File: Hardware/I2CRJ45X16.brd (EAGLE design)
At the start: 146 x 50 mm, 90 parts, among them IC1 MCP23017SO, IC2 MCP23017SO, IC3 MCP23017SO, IC4 MCP23017SO, J1 RJ45-X8, J2 RJ45-X8, J4 I2C-BREAKOUT, J6 I2C-BREAKOUT

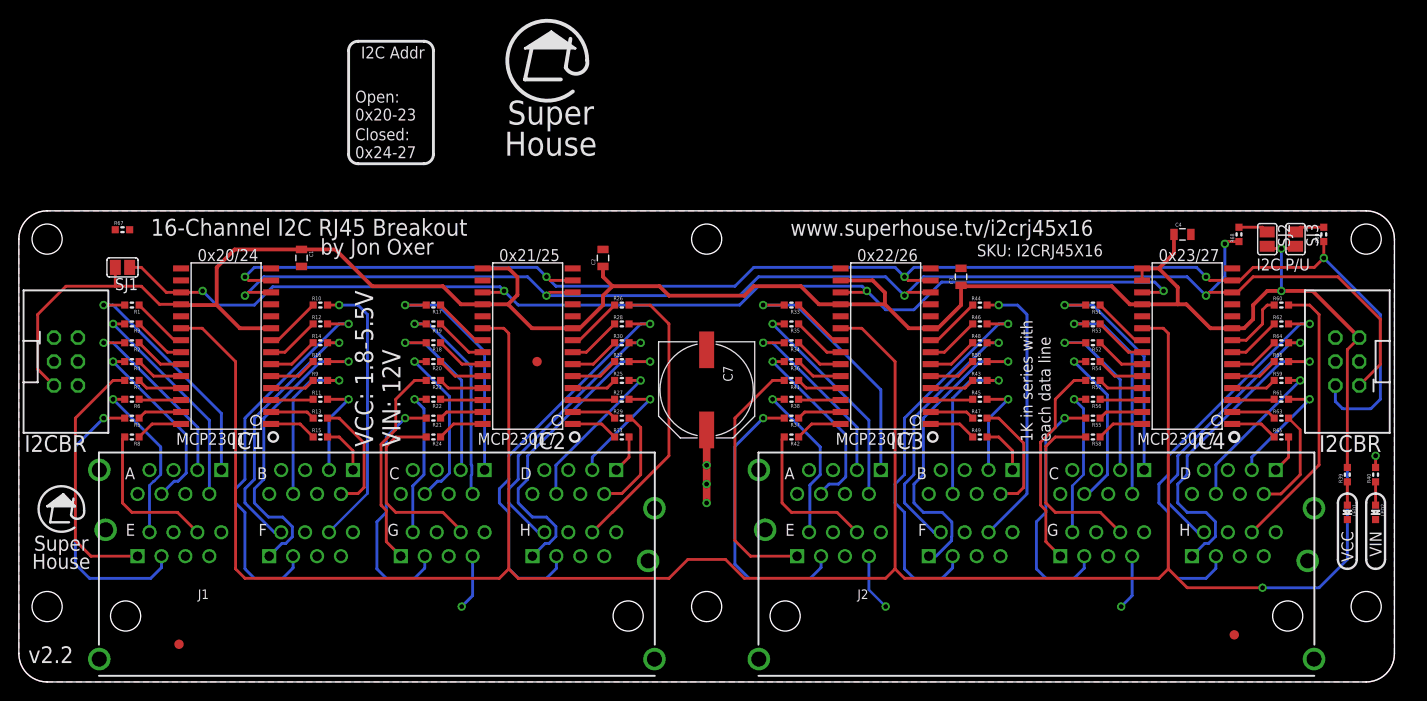
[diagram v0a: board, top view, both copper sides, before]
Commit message: Replaced project files with major redesign for v3.0 release.
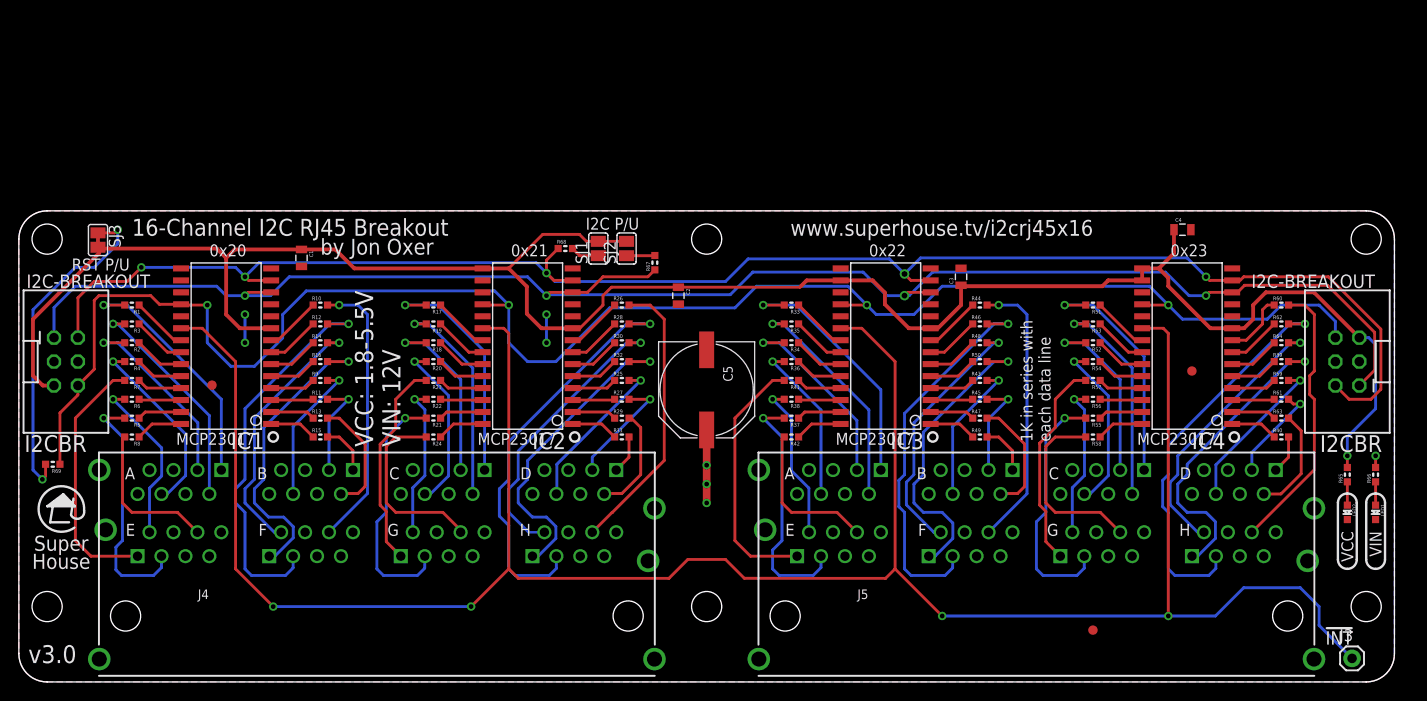
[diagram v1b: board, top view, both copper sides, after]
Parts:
- removed J6: I2C-BREAKOUT, SuperHouse-Connectors:2X03-SHROUDED
- added J3: M01-PLAIN, SuperHouse-Connectors:1X01
- added J5: RJ45-X8, SuperHouse-Connectors:RJ45-2X4
- C5: value 330uF -> 330uF 50V
- FID1, FID2, FID3: device freetronics:FIDUCIAL-1X2.5 -> SuperHouse-Symbols:FIDUCIAL-1X2.5
- J1, J2: value RJ45-X8 -> I2C-BREAKOUT; device SuperHouse-Connectors:RJ45-2X4 -> SuperHouse-Connectors:2X03-SHROUDED
- J4: value I2C-BREAKOUT -> RJ45-X8; device SuperHouse-Connectors:2X03-SHROUDED -> SuperHouse-Connectors:RJ45-2X4
- LED1: value BLUE -> GREEN
- LED2: value GREEN -> BLUE
- R39, R40: value 4K7 -> 1K
- R65, R66: value 1K -> 4K7
- R67, R68: value 10K -> 4K7
- R69: value 10K -> 22K
- SJ1: value I2C Address -> SDA PU
- SJ3: value SDA PU -> RST-PU; device SuperHouse-Jumpers:SJ -> SuperHouse-Jumpers:SJC
- moved R69 137.1 mm to (3.60, 23.1), turned to 180 degrees
- moved SJ3 127.1 mm to (8.40, 46.9)
- moved FID1 111.7 mm to (20.5, 31.5)
- moved FID2 111.3 mm to (124.5, 33.0)
- moved R68 71.5 mm to (58.0, 46.0), turned to 0 degrees
- moved SJ2 68.0 mm to (64.5, 46.0), turned to 90 degrees
- moved FID3 65.5 mm to (114.0, 5.50)
- moved R67 56.6 mm to (67.5, 44.5), turned to 90 degrees
- moved SJ1 50.5 mm to (61.5, 46.0), turned to 90 degrees
- moved J1 42.6 mm to (5.00, 34.0)
- moved J2 42.6 mm to (141.0, 34.0), turned to 180 degrees
- moved J4 42.6 mm to (38.0, 7.00)
- moved R66 15.6 mm to (144.0, 22.0), turned to 90 degrees
- moved R39 13.9 mm to (134.0, 34.0), turned to 0 degrees
- moved R40 10.8 mm to (134.0, 26.0), turned to 0 degrees
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- renumbered C7 to C5
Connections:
- removed net ADDR2: IC1.17, IC2.17, IC3.17, IC4.17, R67.2, SJ1.1
- new net N$2: R68.2, SJ1.1
- net !INT: now also J3.1
- net !RESET: now also IC1.18, IC2.18, IC3.18, IC4.18, J1.6, J2.6, R69.1; no longer J4.6, J6.6
- net 1A1: now also J4.A1; no longer J1.A1
- net 1A2: now also J4.A2; no longer J1.A2
- net 1A3: now also J4.A3; no longer J1.A3
- net 1A6: now also J4.A6; no longer J1.A6
- net 1B1: now also J4.B1; no longer J1.B1
- net 1B2: now also J4.B2; no longer J1.B2
- net 1B3: now also J4.B3; no longer J1.B3
- net 1B6: now also J4.B6; no longer J1.B6
- net 1C1: now also J4.C1; no longer J1.C1
- net 1C2: now also J4.C2; no longer J1.C2
- net 1C3: now also J4.C3; no longer J1.C3
- net 1C6: now also J4.C6; no longer J1.C6
- net 1D1: now also J4.D1; no longer J1.D1
- net 1D2: now also J4.D2; no longer J1.D2
- net 1D3: now also J4.D3; no longer J1.D3
- net 1D6: now also J4.D6; no longer J1.D6
- net 1E1: now also J4.E1; no longer J1.E1
- net 1E2: now also J4.E2; no longer J1.E2
- net 1E3: now also J4.E3; no longer J1.E3
- net 1E6: now also J4.E6; no longer J1.E6
- net 1F1: now also J4.F1; no longer J1.F1
- net 1F2: now also J4.F2; no longer J1.F2
- net 1F3: now also J4.F3; no longer J1.F3
- net 1F6: now also J4.F6; no longer J1.F6
- net 1G1: now also J4.G1; no longer J1.G1
- net 1G2: now also J4.G2; no longer J1.G2
- net 1G3: now also J4.G3; no longer J1.G3
- net 1G6: now also J4.G6; no longer J1.G6
- net 1H1: now also J4.H1; no longer J1.H1
- net 1H2: now also J4.H2; no longer J1.H2
- net 1H3: now also J4.H3; no longer J1.H3
- net 1H6: now also J4.H6; no longer J1.H6
- net 2A1: now also J5.A1; no longer J2.A1
- net 2A2: now also J5.A2; no longer J2.A2
- net 2A3: now also J5.A3; no longer J2.A3
- net 2A6: now also J5.A6; no longer J2.A6
- net 2B1: now also J5.B1; no longer J2.B1
- net 2B2: now also J5.B2; no longer J2.B2
- net 2B3: now also J5.B3; no longer J2.B3
- net 2B6: now also J5.B6; no longer J2.B6
- net 2C1: now also J5.C1; no longer J2.C1
- net 2C2: now also J5.C2; no longer J2.C2
- net 2C3: now also J5.C3; no longer J2.C3
- net 2C6: now also J5.C6; no longer J2.C6
- net 2D1: now also J5.D1, R40.2; no longer J2.D1, R65.2
- net 2D2: now also J5.D2; no longer J2.D2
- net 2D3: now also J5.D3; no longer J2.D3
- net 2D6: now also J5.D6; no longer J2.D6
- net 2E1: now also J5.E1; no longer J2.E1
- net 2E2: now also J5.E2; no longer J2.E2
- net 2E3: now also J5.E3; no longer J2.E3
- net 2E6: now also J5.E6; no longer J2.E6
- net 2F1: now also J5.F1; no longer J2.F1
- net 2F2: now also J5.F2; no longer J2.F2
- net 2F3: now also J5.F3; no longer J2.F3
- net 2F6: now also J5.F6; no longer J2.F6
- net 2G1: now also J5.G1; no longer J2.G1
- net 2G2: now also J5.G2; no longer J2.G2
- net 2G3: now also J5.G3; no longer J2.G3
- net 2G6: now also J5.G6; no longer J2.G6
- net 2H1: now also J5.H1, R39.2; no longer J2.H1, R66.2
- net 2H2: now also J5.H2; no longer J2.H2
- net 2H3: now also J5.H3; no longer J2.H3
- net 2H6: now also J5.H6; no longer J2.H6
- net GND: now also IC1.17, IC2.17, IC3.17, IC4.17, J1.4, J2.4, J4.A7, J4.A8, J4.B7, J4.B8, J4.C7, J4.C8, J4.D7, J4.D8, J4.E7, J4.E8, J4.F7, J4.F8, J4.G7, J4.G8, J4.GND0, J4.GND1, J4.GND2, J4.GND3, J4.GND4, J4.GND5, J4.H7, J4.H8, J5.A7, J5.A8, J5.B7, J5.B8, J5.C7, J5.C8, J5.D7, J5.D8, J5.E7, J5.E8, J5.F7, J5.F8, J5.G7, J5.G8, J5.GND0, J5.GND1, J5.GND2, J5.GND3, J5.GND4, J5.GND5, J5.H7, J5.H8; no longer J1.A7, J1.A8, J1.B7, J1.B8, J1.C7, J1.C8, J1.D7, J1.D8, J1.E7, J1.E8, J1.F7, J1.F8, J1.G7, J1.G8, J1.GND0, J1.GND1, J1.GND2, J1.GND3, J1.GND4, J1.GND5, J1.H7, J1.H8, J2.A7, J2.A8, J2.B7, J2.B8, J2.C7, J2.C8, J2.D7, J2.D8, J2.E7, J2.E8, J2.F7, J2.F8, J2.G7, J2.G8, J2.GND0, J2.GND1, J2.GND2, J2.GND3, J2.GND4, J2.GND5, J2.H7, J2.H8, J4.4, J6.4, R67.1
- net GPB0-4: now also R40.1; no longer R65.1
- net GPB4-4: now also R39.1; no longer R66.1
- net N$1: now also R67.2; no longer R68.2
- net N$7: now also LED2.A, R65.1; no longer LED1.A, R39.1
- net N$8: now also LED1.A, R66.1; no longer LED2.A, R40.1
- net SCL: now also J1.1, J2.1, R67.1; no longer J4.1, J6.1, R68.1
- net SDA: now also J1.2, J2.2, R68.1; no longer J4.2, J6.2, R69.1
- net VCC: now also J1.5, J2.5, R65.2; no longer IC1.18, IC2.18, IC3.18, IC4.18, J4.5, J6.5, R39.2
- net VIN: now also J1.3, J2.3, J4.A4, J4.A5, J4.B4, J4.B5, J4.C4, J4.C5, J4.D4, J4.D5, J4.E4, J4.E5, J4.F4, J4.F5, J4.G4, J4.G5, J4.H4, J4.H5, J5.A4, J5.A5, J5.B4, J5.B5, J5.C4, J5.C5, J5.D4, J5.D5, J5.E4, J5.E5, J5.F4, J5.F5, J5.G4, J5.G5, J5.H4, J5.H5, R66.2; no longer J1.A4, J1.A5, J1.B4, J1.B5, J1.C4, J1.C5, J1.D4, J1.D5, J1.E4, J1.E5, J1.F4, J1.F5, J1.G4, J1.G5, J1.H4, J1.H5, J2.A4, J2.A5, J2.B4, J2.B5, J2.C4, J2.C5, J2.D4, J2.D5, J2.E4, J2.E5, J2.F4, J2.F5, J2.G4, J2.G5, J2.H4, J2.H5, J4.3, J6.3, R40.2
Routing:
- net !RESET: track 0.00 -> 185.3 mm, vias 0 -> 4
- net ADDR2: track 124.1 -> 0.00 mm, vias 4 -> 0
- net N$3: track 3.21 -> 35.8 mm, vias 0 -> 2
- net SCL: track 152.8 -> 177.8 mm, vias 5 -> 4
- net SDA: track 154.2 -> 176.0 mm
- net GND: track 17.7 -> 6.00 mm, vias 3 -> 4
- net VCC: track 232.7 -> 223.5 mm, vias 2 -> 1
- net 1E3: track 30.4 -> 26.1 mm
- net 2E3: track 30.4 -> 26.5 mm
- net N$2: track 0.00 -> 3.05 mm
- net 2A6: track 20.2 -> 17.4 mm
- net 2B6: track 17.1 -> 15.3 mm
- net 1B6: track 17.1 -> 15.3 mm
- net 2D3: track 12.3 -> 10.6 mm
- net 2H1: track 34.5 -> 33.1 mm
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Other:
- board text added: "!INT"
- board text added: "!RST"
- board text added: "0x20"
- board text added: "0x21"
- board text added: "0x22"
- board text added: "0x23"
- board text added: "24-Channel I2C RJ45 Breakout"
- board text added: "Copyright 2019-2021 SuperHouse Automation Pty Ltd Released under the terms of the TAPR Open Hardware License: www.tapr.org/OHL"
- board text added: "GND"
- board text added: "I2C-BREAKOUT"
- board text added: "RJ45 Pinout"
- board text added: "RST P/U"
- board text added: "SCL"
- board text added: "SDA"
- board text added: "v3.0"
- board text added: "www.superhouse.tv"
- board text removed: "0x20/24"
- board text removed: "0x21/25"
- board text removed: "0x22/26"
- board text removed: "0x23/27"
- board text removed: "Closed: 0x24-27"
- board text removed: "Copyright 2019 SuperHouse Automation Pty Ltd Released under the terms of the TAPR Open Hardware License: www.tapr.org/OHL"
- board text removed: "I2C Addr"
- board text removed: "Open: 0x20-23"
- board text removed: "RJ45 Pinout:"
- board text removed: "v2.2"

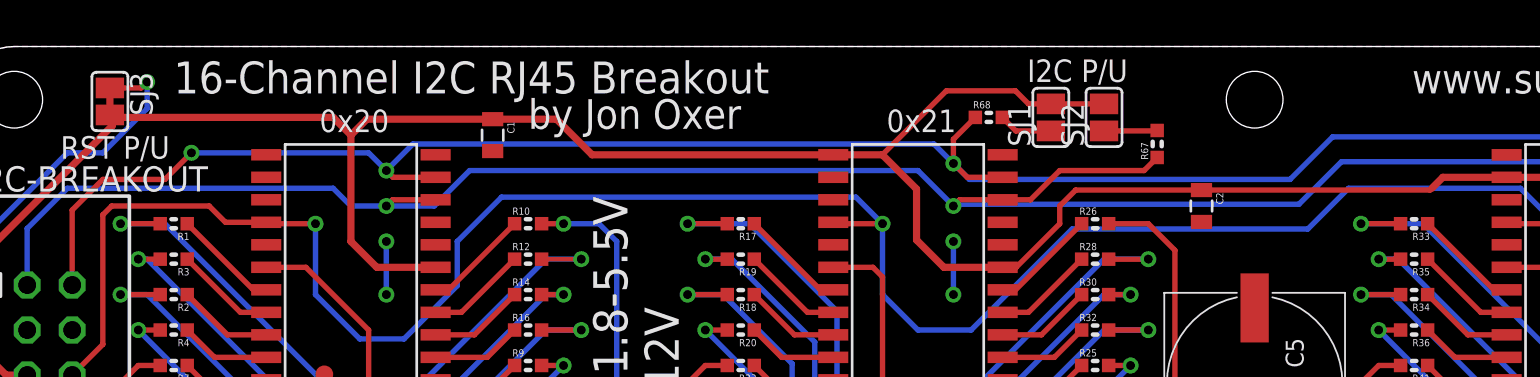
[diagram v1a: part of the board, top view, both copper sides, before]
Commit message: Major rework based on 24-port version.
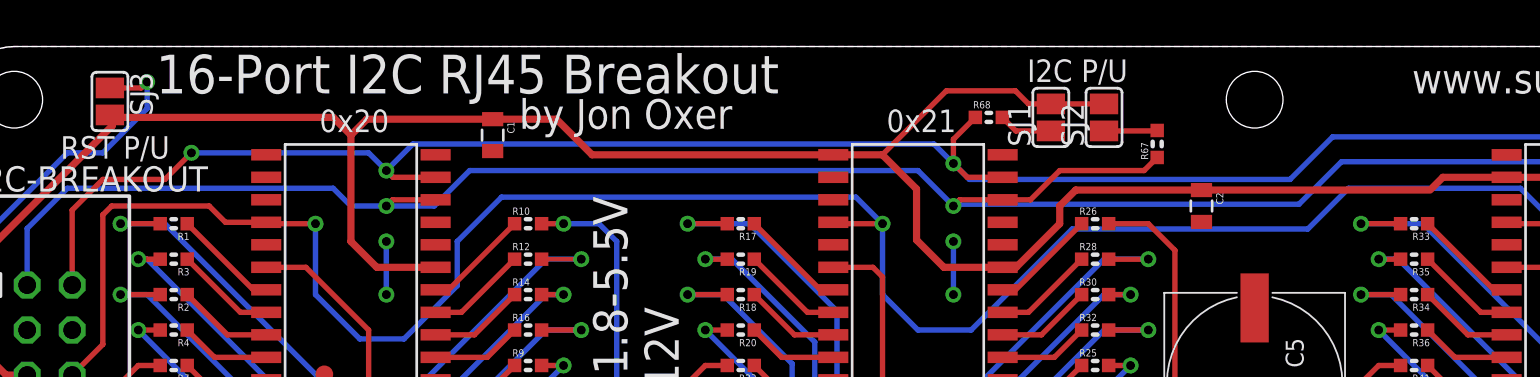
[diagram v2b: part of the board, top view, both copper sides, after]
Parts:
- R69: value 22K -> 10K
- SJ3: device SuperHouse-Jumpers:SJC -> SuperHouse-Jumpers:SJ
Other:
- board text added: "16-Port I2C RJ45 Breakout"
- board text removed: "16-Channel I2C RJ45 Breakout"
- board text removed: "24-Channel I2C RJ45 Breakout"
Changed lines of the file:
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@@
 </layers>
 <board>
-<fusionsync huburn="a.cGVyc29uYWw6dWUyZDliZmNi" projecturn="a.cGVyc29uYWw6dWUyZDliZmNiIzIwMTkwMzE1MTgyMjY5OTA2" f3durn="urn:adsk.wipprod:dm.lineage:_H2PRmvNSomCkomNSTRBxw" pcbguid="e014f554-0983-42e7-88b6-f6e08b18e2c7" lastpulledtime="" lastsyncedchangeguid="1491f9b9-a179-9c0a-9821-19275fe4b9b0" latestrevisionid="" lastsyncedrevisionid="" lastboardhashguid="57911f44-b240-5674-ec1f-8acbffdfcb08" lastpushedtime="2021-04-15T04:03:47Z" linktopcb3d="false"/>
+<fusionsync huburn="a.cGVyc29uYWw6dWUyZDliZmNi" projecturn="a.cGVyc29uYWw6dWUyZDliZmNiIzIwMTkwMzE1MTgyMjY5OTA2" f3durn="urn:adsk.wipprod:dm.lineage:_H2PRmvNSomCkomNSTRBxw" pcbguid="e014f554-0983-42e7-88b6-f6e08b18e2c7" lastpulledtime="" lastsyncedchangeguid="1491f9b9-a179-9c0a-9821-19275fe4b9b0" latestrevisionid="" lastsyncedrevisionid="" lastboardhashguid="9f721456-5d46-4459-276f-f39935e09a9c" lastpushedtime="2021-04-15T05:54:07Z" linktopcb3d="false"/>
 <plain>
 <wire x1="3" y1="0" x2="0" y2="3" width="0" layer="20" curve="-90"/>
@@
 <text x="50.045" y="43.854" size="3.1" layer="22" font="vector" ratio="17" distance="30" rot="MR0" align="center-left">Super
 House</text>
-<text x="60.045" y="27" size="2.8" layer="22" font="vector" ratio="17" distance="20" rot="MR0">24-Channel
+<text x="60.045" y="27" size="2.8" layer="22" font="vector" ratio="17" distance="20" rot="MR0">16-Port
 I2C RJ45
 Breakout</text>
@@
 <text x="4.5" y="12" size="1.6" layer="21" font="vector" ratio="17" distance="20" align="bottom-center">Super
 House</text>
-<text x="12" y="47.354" size="1.8" layer="21" font="vector" ratio="17" distance="30">16-Channel I2C RJ45 Breakout</text>
-<text x="32" y="45.354" size="1.6764" layer="21" font="vector" ratio="17" distance="30">by Jon Oxer</text>
+<text x="11" y="47.354" size="2.1844" layer="21" font="vector" ratio="17" distance="30">16-Port I2C RJ45 Breakout</text>
+<text x="31.5" y="45.354" size="1.6764" layer="21" font="vector" ratio="17" distance="30">by Jon Oxer</text>
 <text x="40.5" y="24.955" size="1.9304" layer="21" font="vector" ratio="17" rot="R90">VCC: 1.8-5.5V
 VIN: 12V</text>
@@
 <attribute name="VALUE" x="122.484" y="46.603" size="0.4064" layer="27"/>
 </element>
-<element name="SJ2" library="SuperHouse-Jumpers" library_urn="urn:adsk.eagle:library:12190622" package="SJ" package3d_urn="urn:adsk.eagle:package:7066338/1" value="SCL PU" x="64.5" y="46" smashed="yes" rot="R90">
+<element name="SJ2" library="SuperHouse-Jumpers" library_urn="urn:adsk.eagle:library:12190622" package="SJ" package3d_urn="urn:adsk.eagle:package:7066338/2" value="SCL PU" x="64.5" y="46" smashed="yes" rot="R90">
 <attribute name="NAME" x="63.357" y="44.349" size="1.27" layer="25" ratio="10" rot="R90"/>
 <attribute name="VALUE" x="64.5" y="46.4001" size="0.02" layer="27" rot="R90"/>
 </element>
-<element name="SJ1" library="SuperHouse-Jumpers" library_urn="urn:adsk.eagle:library:12190622" package="SJ" package3d_urn="urn:adsk.eagle:package:7066338/1" value="SDA PU" x="61.5" y="46" smashed="yes" rot="R90">
+<element name="SJ1" library="SuperHouse-Jumpers" library_urn="urn:adsk.eagle:library:12190622" package="SJ" package3d_urn="urn:adsk.eagle:package:7066338/2" value="SDA PU" x="61.5" y="46" smashed="yes" rot="R90">
 <attribute name="NAME" x="60.357" y="44.349" size="1.27" layer="25" ratio="10" rot="R90"/>
 <attribute name="VALUE" x="61.5" y="46.4001" size="0.02" layer="27" rot="R90"/>
@@
 <attribute name="VALUE" x="144.9652" y="20.984" size="0.4064" layer="27" font="vector" rot="R90"/>
 </element>
-<element name="R69" library="SuperHouse-DiscreteSemi" library_urn="urn:adsk.eagle:library:11768461" package="R0603" package3d_urn="urn:adsk.eagle:package:11768543/2" value="22K" x="3.6" y="23.1" smashed="yes" rot="R180">
+<element name="R69" library="SuperHouse-DiscreteSemi" library_urn="urn:adsk.eagle:library:11768461" package="R0603" package3d_urn="urn:adsk.eagle:package:11768543/2" value="10K" x="3.6" y="23.1" smashed="yes" rot="R180">
 <attribute name="NAME" x="4.489" y="22.592" size="0.4064" layer="25" font="vector" rot="R180"/>
 <attribute name="VALUE" x="4.616" y="24.0652" size="0.4064" layer="27" font="vector" rot="R180"/>
 </element>
-<element name="SJ3" library="SuperHouse-Jumpers" library_urn="urn:adsk.eagle:library:12190622" package="SJC" package3d_urn="urn:adsk.eagle:package:7066342/2" value="RST-PU" x="8.4" y="46.9" smashed="yes" rot="R270">
+<element name="SJ3" library="SuperHouse-Jumpers" library_urn="urn:adsk.eagle:library:12190622" package="SJ" package3d_urn="urn:adsk.eagle:package:7066338/2" value="RST-PU" x="8.4" y="46.9" smashed="yes" rot="R270">
 <attribute name="NAME" x="9.543" y="48.551" size="1.27" layer="25" ratio="10" rot="R270"/>
 <attribute name="VALUE" x="8.4" y="46.4999" size="0.02" layer="27" rot="R270"/>
@@
 <wire x1="115.62" y1="42.62" x2="115" y2="42" width="0.4064" layer="1"/>
 <wire x1="83" y1="42" x2="82.9" y2="41.9" width="0.3048" layer="1"/>
-<wire x1="82.9" y1="41.9" x2="70" y2="41.9" width="0.3048" layer="1"/>
-<wire x1="70" y1="41.9" x2="62.9" y2="41.9" width="0.3048" layer="1"/>
-<wire x1="62.9" y1="41.9" x2="62" y2="41" width="0.3048" layer="1"/>
-<wire x1="62" y1="41" x2="62" y2="40" width="0.3048" layer="1"/>
-<wire x1="62" y1="40" x2="59.54" y2="37.54" width="0.3048" layer="1"/>
-<wire x1="59.54" y1="37.54" x2="58.78" y2="37.54" width="0.3048" layer="1"/>
+<wire x1="82.9" y1="41.9" x2="70" y2="41.9" width="0.4064" layer="1"/>
+<wire x1="70" y1="41.9" x2="62.9" y2="41.9" width="0.4064" layer="1"/>
+<wire x1="62.9" y1="41.9" x2="62" y2="41" width="0.4064" layer="1"/>
+<wire x1="62" y1="41" x2="62" y2="40" width="0.4064" layer="1"/>
+<wire x1="62" y1="40" x2="59.54" y2="37.54" width="0.4064" layer="1"/>
+<wire x1="59.54" y1="37.54" x2="58.78" y2="37.54" width="0.4064" layer="1"/>
 <wire x1="64.5" y1="46.762" x2="61.5" y2="46.762" width="0.3048" layer="1"/>
 <wire x1="61.5" y1="46.762" x2="60.238" y2="46.762" width="0.3048" layer="1"/>
@@
 <mfgpreviewcolor name="substratecolor" color="0xFF786E46"/>
 </mfgpreviewcolors>
-<errors>
-</errors>
 </board>
 </drawing>
